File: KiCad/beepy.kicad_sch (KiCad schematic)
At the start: 102 parts, among them J1 FDX0019B1, J10 FDX0019B1, J11 FDX0019B1, J12 FDX0019B1, J13 FDX0019B1, J14 FDX0019B1, J15 USB_C_Receptacle_USB2.0, J16 FDX0019B1, J17 FDX0019B1, J18 FDX0019B1, J19 FDX0019B1, J2 FDX0019B1, J20 FDX0019B1, J21 FDX0019B1, J22 Pi Zero, J23 FDX0019B1, J24 FDX0019B1, J25 FDX0019B1, J26 FDX0019B1, J27 FDX0019B1, J28 FDX0019B1, J29 FDX0019B1, J3 FDX0019B1, J30 FDX0019B1, J31 FDX0019B1, J32 FDX0019B1, J33 FDX0019B1, J34 FDX0019B1, J35 FDX0019B1, J36 FDX0019B1, J37 FDX0019B1, J38 FDX0019B1, J39 FDX0019B1, J4 FDX0019B1, J40 FDX0019B1, J41 FDX0019B1, J42 FDX0019B1, J43 Battery, J44 Header 1, J45 PRG_HEADER, J46 Header 2, J47 Header 3, J5 FDX0019B1, J6 FDX0019B1, J7 FDX0019B1, J8 FDX0019B1, J9 FDX0019B1, Q1 SI2301, Q2 SI2301, Q9 S8050, SW1 ON/OFF, SW2 Button, U1 TP4054, U2 TPS61090, U3 LS027B7DH01

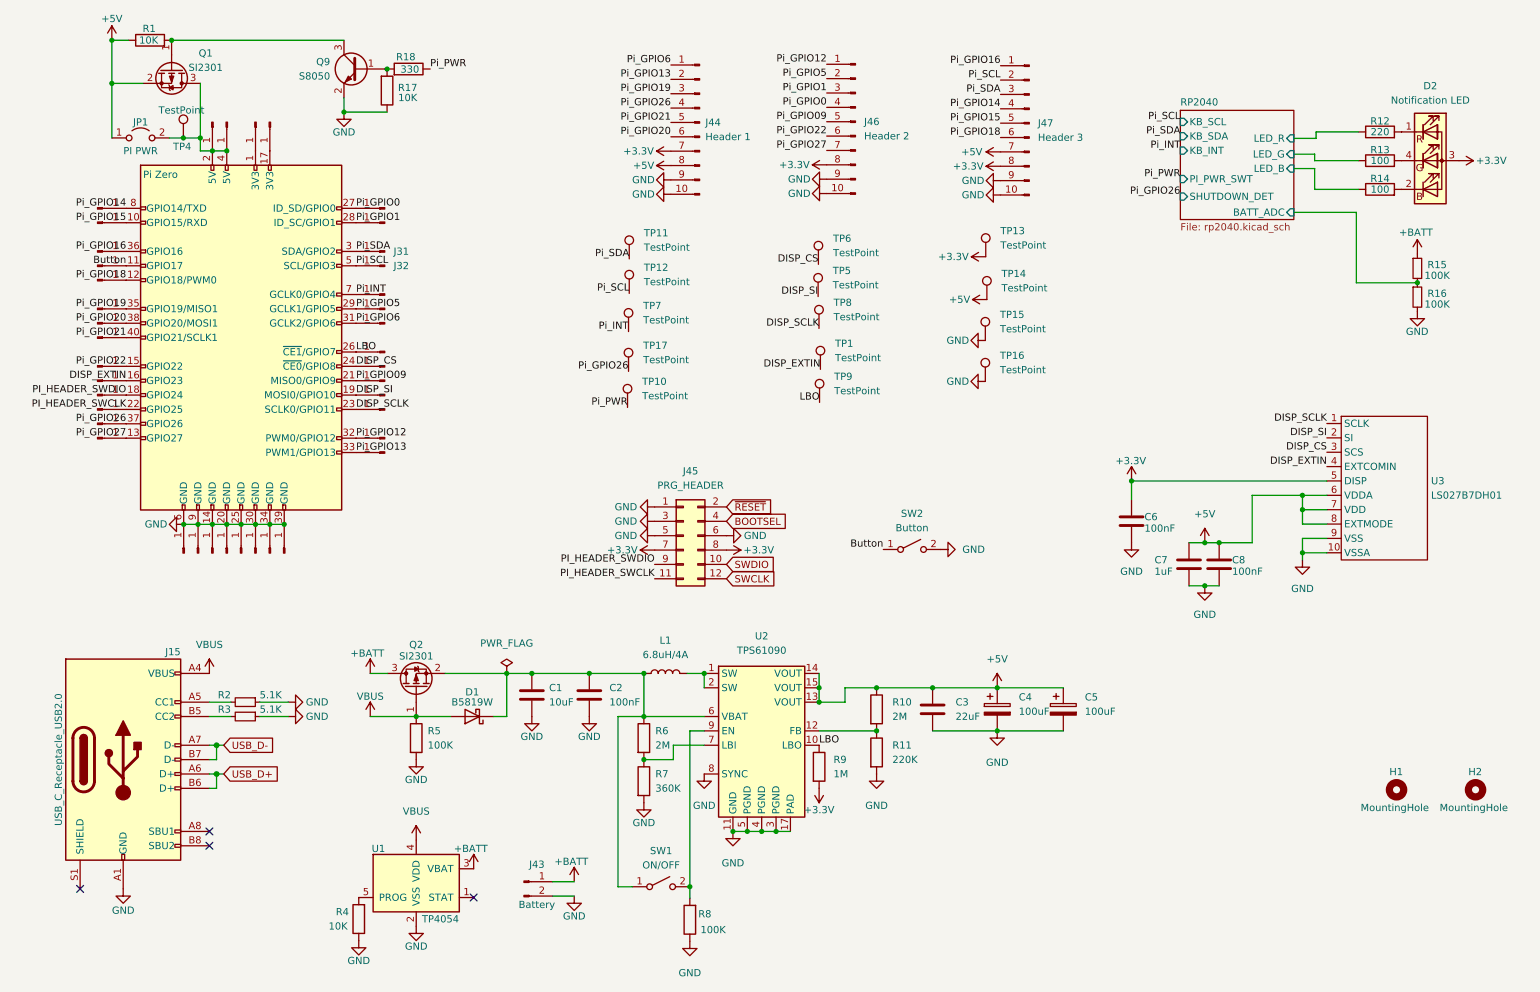
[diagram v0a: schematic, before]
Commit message: Moved 4 layers to 2 layers with ground fill
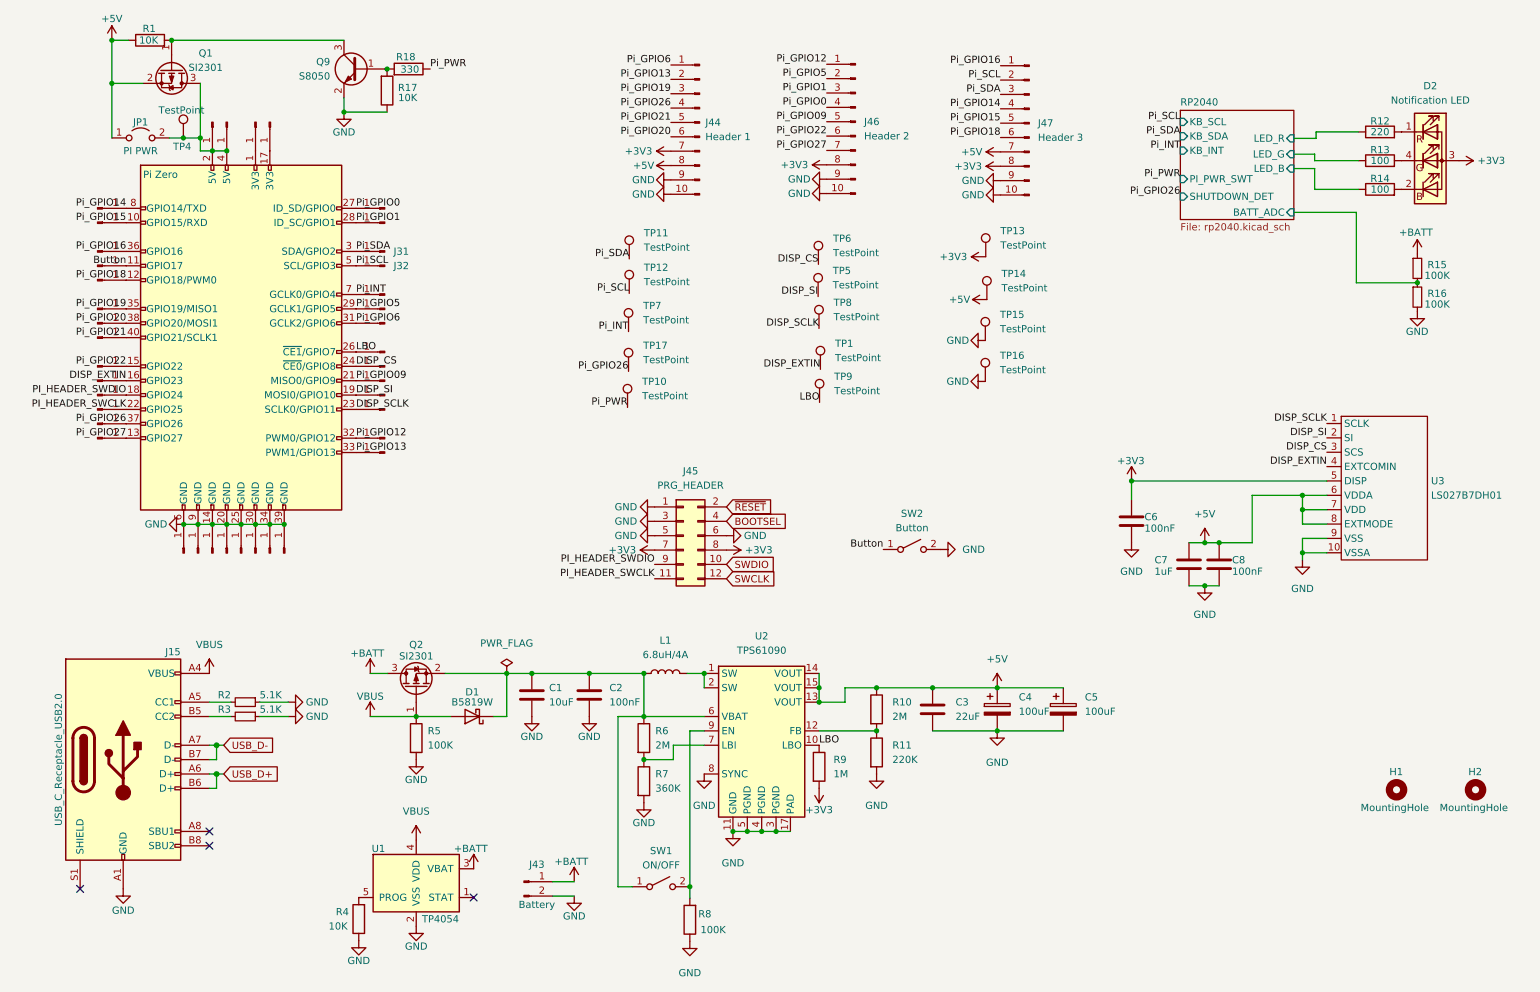
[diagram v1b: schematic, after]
